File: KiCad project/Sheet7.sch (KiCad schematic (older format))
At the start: 17 parts, among them U6 AFE4403, X4 CRYSTAL_8MHZ_SMD

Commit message: New packages, PCB
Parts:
- C26: renamed from C37; footprint (none) -> Capacitors_SMD:C_0603
- C27: renamed from C38; footprint (none) -> Capacitors_SMD:C_0603
- C28, C29: renamed from C?; footprint (none) -> Capacitors_SMD:C_0603
- C30: renamed from C39; footprint (none) -> Capacitors_SMD:C_0603
- C31: renamed from C40; footprint (none) -> Capacitors_SMD:C_0603
- C32: renamed from C41; footprint (none) -> Capacitors_SMD:C_0603
- C33: renamed from C42; footprint (none) -> Capacitors_SMD:C_0603
- C34: renamed from C43; footprint (none) -> Capacitors_SMD:C_0603
- C35: renamed from C44; footprint (none) -> Capacitors_SMD:C_0603
- FB1: renamed from FB?; footprint (none) -> Capacitors_SMD:C_0603
- R7: footprint (none) -> Resistors_SMD:R_0603
- X3: renamed from X4; footprint (none) -> Anastasia:5x3.2_Crystal_SMD
- renumbered U6 to U7
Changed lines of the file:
@@
 $EndDescr
 $Comp
-L AFE4403 U6
+L AFE4403 U7
 U 1 1 5507E4DD
 P 4850 2000
-F 0 "U6" H 4900 2050 60  0000 C CNN
+F 0 "U7" H 4900 2050 60  0000 C CNN
 F 1 "AFE4403" H 6300 -350 60  0000 C CNN
 F 2 "Anastasia:DSBGA36" H 4850 2000 60  0001 C CNN
@@
 $EndComp
 $Comp
-L CRYSTAL_SMD X4
+L CRYSTAL_SMD X3
 U 1 1 5507E5E4
 P 7200 3700
-F 0 "X4" H 7200 3790 50  0000 C CNN
+F 0 "X3" H 7200 3790 50  0000 C CNN
 F 1 "CRYSTAL_8MHZ_SMD" H 7230 3590 50  0000 L CNN
-F 2 "" H 7200 3700 60  0001 C CNN
+F 2 "Anastasia:5x3.2_Crystal_SMD" H 7200 3700 60  0001 C CNN
 F 3 "" H 7200 3700 60  0000 C CNN
 	1    7200 3700
@@
 $EndComp
 $Comp
-L GND #PWR033
+L GND #PWR032
 U 1 1 5507E63E
 P 7200 4300
-F 0 "#PWR033" H 7200 4050 60  0001 C CNN
+F 0 "#PWR032" H 7200 4050 60  0001 C CNN
 F 1 "GND" H 7200 4150 60  0000 C CNN
 F 2 "" H 7200 4300 60  0000 C CNN
@@
 $EndComp
 $Comp
-L C C43
+L C C34
 U 1 1 5507E652
 P 7000 4050
-F 0 "C43" H 7050 4150 50  0000 L CNN
+F 0 "C34" H 7050 4150 50  0000 L CNN
 F 1 "C" H 7050 3950 50  0000 L CNN
-F 2 "" H 7038 3900 30  0001 C CNN
+F 2 "Capacitors_SMD:C_0603" H 7038 3900 30  0001 C CNN
 F 3 "" H 7000 4050 60  0000 C CNN
 	1    7000 4050
@@
 $EndComp
 $Comp
-L C C44
+L C C35
 U 1 1 5507E675
 P 7400 4050
-F 0 "C44" H 7450 4150 50  0000 L CNN
+F 0 "C35" H 7450 4150 50  0000 L CNN
 F 1 "C" H 7450 3950 50  0000 L CNN
-F 2 "" H 7438 3900 30  0001 C CNN
+F 2 "Capacitors_SMD:C_0603" H 7438 3900 30  0001 C CNN
 F 3 "" H 7400 4050 60  0000 C CNN
 	1    7400 4050
@@
 Choose load capacitors according \nto crystal's datasheet\n
 $Comp
-L GND #PWR034
+L GND #PWR033
 U 1 1 5507E970
 P 7050 3350
-F 0 "#PWR034" H 7050 3100 60  0001 C CNN
+F 0 "#PWR033" H 7050 3100 60  0001 C CNN
 F 1 "GND" H 7050 3200 60  0000 C CNN
 F 2 "" H 7050 3350 60  0000 C CNN
@@
 $EndComp
 $Comp
-L GND #PWR035
+L GND #PWR034
 U 1 1 5507E997
 P 6900 2800
-F 0 "#PWR035" H 6900 2550 60  0001 C CNN
+F 0 "#PWR034" H 6900 2550 60  0001 C CNN
 F 1 "GND" H 6900 2650 60  0000 C CNN
 F 2 "" H 6900 2800 60  0000 C CNN
@@
 $EndComp
 $Comp
-L +3V3 #PWR036
+L +3V3 #PWR035
 U 1 1 5507E9AF
 P 8450 2550
-F 0 "#PWR036" H 8450 2400 60  0001 C CNN
+F 0 "#PWR035" H 8450 2400 60  0001 C CNN
 F 1 "+3V3" H 8450 2690 60  0000 C CNN
 F 2 "" H 8450 2550 60  0000 C CNN
@@
 $EndComp
 $Comp
-L C C42
+L C C33
 U 1 1 5507EA21
 P 7800 3550
-F 0 "C42" H 7850 3650 50  0000 L CNN
+F 0 "C33" H 7850 3650 50  0000 L CNN
 F 1 "2.2U" H 7850 3450 50  0000 L CNN
-F 2 "" H 7838 3400 30  0001 C CNN
+F 2 "Capacitors_SMD:C_0603" H 7838 3400 30  0001 C CNN
 F 3 "" H 7800 3550 60  0000 C CNN
 	1    7800 3550
@@
 $EndComp
 $Comp
-L GND #PWR037
+L GND #PWR036
 U 1 1 5507EA5D
 P 7800 3850
-F 0 "#PWR037" H 7800 3600 60  0001 C CNN
+F 0 "#PWR036" H 7800 3600 60  0001 C CNN
 F 1 "GND" H 7800 3700 60  0000 C CNN
 F 2 "" H 7800 3850 60  0000 C CNN
@@
 $EndComp
 $Comp
-L C C40
+L C C31
 U 1 1 5507EAF1
 P 8450 2750
-F 0 "C40" H 8500 2850 50  0000 L CNN
+F 0 "C31" H 8500 2850 50  0000 L CNN
 F 1 "0.1U" H 8500 2650 50  0000 L CNN
-F 2 "" H 8488 2600 30  0001 C CNN
+F 2 "Capacitors_SMD:C_0603" H 8488 2600 30  0001 C CNN
 F 3 "" H 8450 2750 60  0000 C CNN
 	1    8450 2750
@@
 $EndComp
 $Comp
-L GND #PWR038
+L GND #PWR037
 U 1 1 5507EB22
 P 8450 3000
-F 0 "#PWR038" H 8450 2750 60  0001 C CNN
+F 0 "#PWR037" H 8450 2750 60  0001 C CNN
 F 1 "GND" H 8450 2850 60  0000 C CNN
 F 2 "" H 8450 3000 60  0000 C CNN
@@
 $EndComp
 $Comp
-L GND #PWR039
+L GND #PWR038
 U 1 1 5507EC48
 P 6950 2450
-F 0 "#PWR039" H 6950 2200 60  0001 C CNN
+F 0 "#PWR038" H 6950 2200 60  0001 C CNN
 F 1 "GND" H 6950 2300 60  0000 C CNN
 F 2 "" H 6950 2450 60  0000 C CNN
@@
 	7100 1850 7100 2650
 $Comp
-L GND #PWR041
+L GND #PWR039
 U 1 1 5507EE1C
 P 7800 2300
-F 0 "#PWR041" H 7800 2050 60  0001 C CNN
+F 0 "#PWR039" H 7800 2050 60  0001 C CNN
 F 1 "GND" H 7800 2150 60  0000 C CNN
 F 2 "" H 7800 2300 60  0000 C CNN
@@
 $EndComp
 $Comp
-L C C39
+L C C30
 U 1 1 5507EE30
 P 7800 2050
-F 0 "C39" H 7850 2150 50  0000 L CNN
+F 0 "C30" H 7850 2150 50  0000 L CNN
 F 1 "0.1U" H 7850 1950 50  0000 L CNN
-F 2 "" H 7838 1900 30  0001 C CNN
+F 2 "Capacitors_SMD:C_0603" H 7838 1900 30  0001 C CNN
 F 3 "" H 7800 2050 60  0000 C CNN
 	1    7800 2050
@@
 	7100 1850 8350 1850
 $Comp
-L C C41
+L C C32
 U 1 1 5507F067
 P 8050 3000
-F 0 "C41" H 8100 3100 50  0000 L CNN
+F 0 "C32" H 8100 3100 50  0000 L CNN
 F 1 "0.1U" H 8100 2900 50  0000 L CNN
-F 2 "" H 8088 2850 30  0001 C CNN
+F 2 "Capacitors_SMD:C_0603" H 8088 2850 30  0001 C CNN
 F 3 "" H 8050 3000 60  0000 C CNN
 	1    8050 3000
@@
 $EndComp
 $Comp
-L GND #PWR042
+L GND #PWR040
 U 1 1 5507F092
 P 8050 3250
-F 0 "#PWR042" H 8050 3000 60  0001 C CNN
+F 0 "#PWR040" H 8050 3000 60  0001 C CNN
 F 1 "GND" H 8050 3100 60  0000 C CNN
 F 2 "" H 8050 3250 60  0000 C CNN
@@
 $EndComp
 $Comp
-L +3V3 #PWR043
+L +3V3 #PWR041
 U 1 1 5507F0A6
 P 8050 2750
-F 0 "#PWR043" H 8050 2600 60  0001 C CNN
+F 0 "#PWR041" H 8050 2600 60  0001 C CNN
 F 1 "+3V3" H 8050 2890 60  0000 C CNN
 F 2 "" H 8050 2750 60  0000 C CNN
@@
 	7700 2800 8050 2800
 $Comp
-L C C37
+L C C26
 U 1 1 5507F407
 P 6850 1450
-F 0 "C37" H 6900 1550 50  0000 L CNN
+F 0 "C26" H 6900 1550 50  0000 L CNN
 F 1 "1U" H 6900 1350 50  0000 L CNN
-F 2 "" H 6888 1300 30  0001 C CNN
+F 2 "Capacitors_SMD:C_0603" H 6888 1300 30  0001 C CNN
 F 3 "" H 6850 1450 60  0000 C CNN
 	1    6850 1450
@@
 $EndComp
 $Comp
-L GND #PWR044
+L GND #PWR042
 U 1 1 5507F42E
 P 6850 1750
-F 0 "#PWR044" H 6850 1500 60  0001 C CNN
+F 0 "#PWR042" H 6850 1500 60  0001 C CNN
 F 1 "GND" H 6850 1600 60  0000 C CNN
 F 2 "" H 6850 1750 60  0000 C CNN
@@
 $EndComp
 $Comp
-L +3V3 #PWR045
+L +3V3 #PWR043
 U 1 1 5507F442
 P 6850 1150
-F 0 "#PWR045" H 6850 1000 60  0001 C CNN
+F 0 "#PWR043" H 6850 1000 60  0001 C CNN
 F 1 "+3V3" H 6850 1290 60  0000 C CNN
 F 2 "" H 6850 1150 60  0000 C CNN
@@
 	6650 1250 6850 1250
 $Comp
-L GND #PWR046
+L GND #PWR044
 U 1 1 5507FE0D
 P 3700 2300
-F 0 "#PWR046" H 3700 2050 60  0001 C CNN
+F 0 "#PWR044" H 3700 2050 60  0001 C CNN
 F 1 "GND" H 3700 2150 60  0000 C CNN
 F 2 "" H 3700 2300 60  0000 C CNN
@@
 $EndComp
 $Comp
-L C C38
+L C C27
 U 1 1 5507FE21
 P 3700 2050
-F 0 "C38" H 3750 2150 50  0000 L CNN
+F 0 "C27" H 3750 2150 50  0000 L CNN
 F 1 "2.2U" H 3750 1950 50  0000 L CNN
-F 2 "" H 3738 1900 30  0001 C CNN
+F 2 "Capacitors_SMD:C_0603" H 3738 1900 30  0001 C CNN
 F 3 "" H 3700 2050 60  0000 C CNN
 	1    3700 2050
@@
 F 0 "R7" V 3080 2350 50  0000 C CNN
 F 1 "10K" V 3007 2351 50  0000 C CNN
-F 2 "" V 2930 2350 30  0001 C CNN
+F 2 "Resistors_SMD:R_0603" V 2930 2350 30  0001 C CNN
 F 3 "" H 3000 2350 30  0000 C CNN
 	1    3000 2350
@@
 Connection ~ 3000 2600
 $Comp
-L +3V3 #PWR047
+L +3V3 #PWR045
 U 1 1 55080B5C
 P 3000 1950
-F 0 "#PWR047" H 3000 1800 60  0001 C CNN
+F 0 "#PWR045" H 3000 1800 60  0001 C CNN
 F 1 "+3V3" H 3000 2090 60  0000 C CNN
 F 2 "" H 3000 1950 60  0000 C CNN
@@
 	3000 2100 3000 1950
 $Comp
-L C C?
+L C C28
 U 1 1 550D75B9
 P 7250 2050
-F 0 "C?" H 7300 2150 50  0000 L CNN
+F 0 "C28" H 7300 2150 50  0000 L CNN
 F 1 "10N" H 7300 1950 50  0000 L CNN
-F 2 "" H 7288 1900 30  0000 C CNN
+F 2 "Capacitors_SMD:C_0603" H 7288 1900 30  0001 C CNN
 F 3 "" H 7250 2050 60  0000 C CNN
 	1    7250 2050
@@
 Connection ~ 7800 1850
 $Comp
-L FILTER FB?
+L FILTER FB1
 U 1 1 550D77C7
 P 8700 1850
-F 0 "FB?" H 8700 2000 50  0000 C CNN
+F 0 "FB1" H 8700 2000 50  0000 C CNN
 F 1 "FILTER" H 8700 1750 50  0000 C CNN
-F 2 "" H 8700 1850 60  0000 C CNN
+F 2 "Capacitors_SMD:C_0603" H 8700 1850 60  0001 C CNN
 F 3 "" H 8700 1850 60  0000 C CNN
 	1    8700 1850
@@
 $EndComp
 $Comp
-L +3V3 #PWR?
+L +3V3 #PWR046
 U 1 1 550D77E4
 P 9200 1700
-F 0 "#PWR?" H 9200 1550 60  0001 C CNN
+F 0 "#PWR046" H 9200 1550 60  0001 C CNN
 F 1 "+3V3" H 9200 1840 60  0000 C CNN
 F 2 "" H 9200 1700 60  0000 C CNN
@@
 Connection ~ 7500 2250
 $Comp
-L C C?
+L C C29
 U 1 1 550D75A0
 P 7500 2050
-F 0 "C?" H 7550 2150 50  0000 L CNN
+F 0 "C29" H 7550 2150 50  0000 L CNN
 F 1 "10N" H 7550 1950 50  0000 L CNN
-F 2 "" H 7538 1900 30  0000 C CNN
+F 2 "Capacitors_SMD:C_0603" H 7538 1900 30  0001 C CNN
 F 3 "" H 7500 2050 60  0000 C CNN
 	1    7500 2050

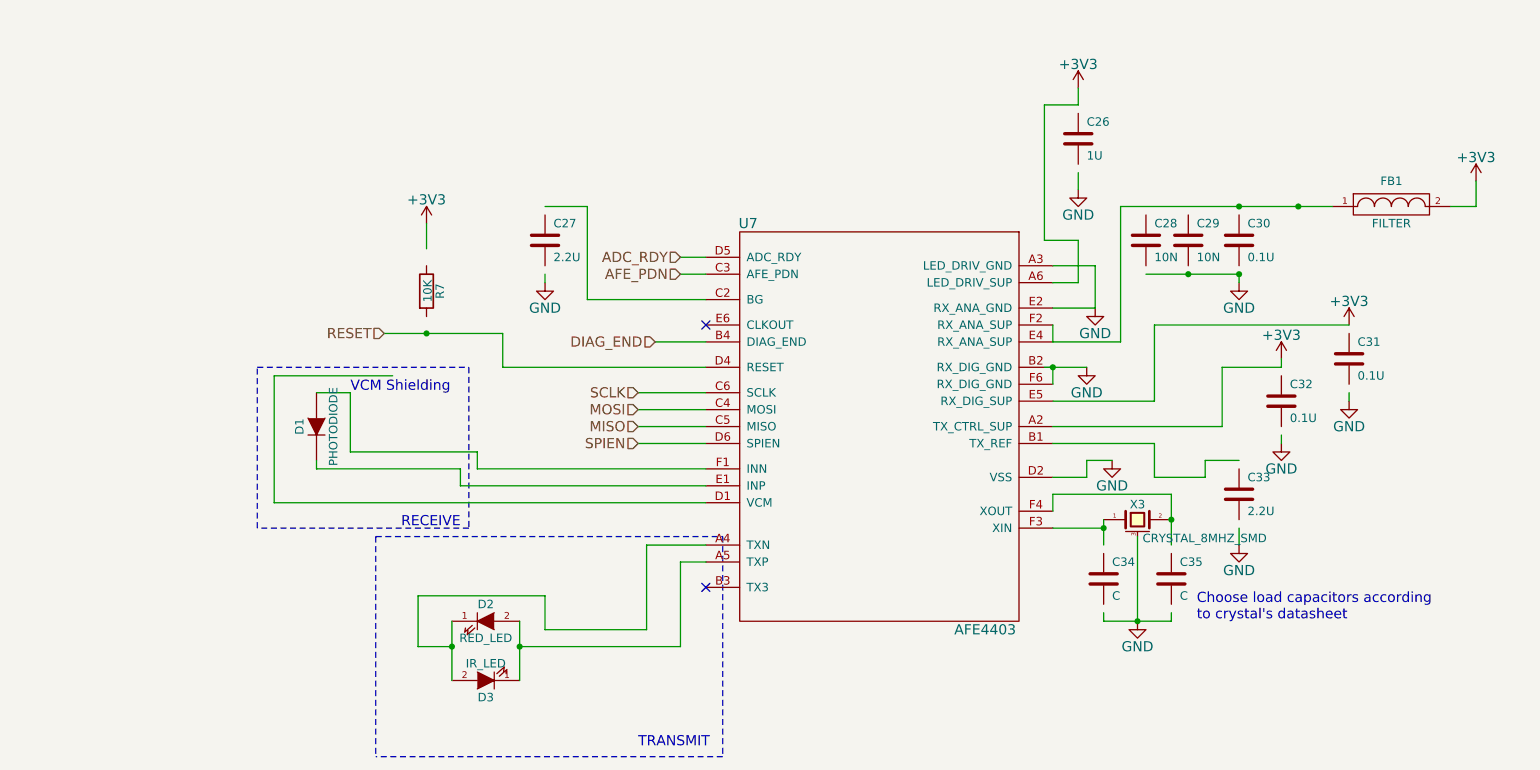
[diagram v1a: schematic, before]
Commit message: Schematics, PCB design
New schematics for the pulse oximeter, PCB layout design
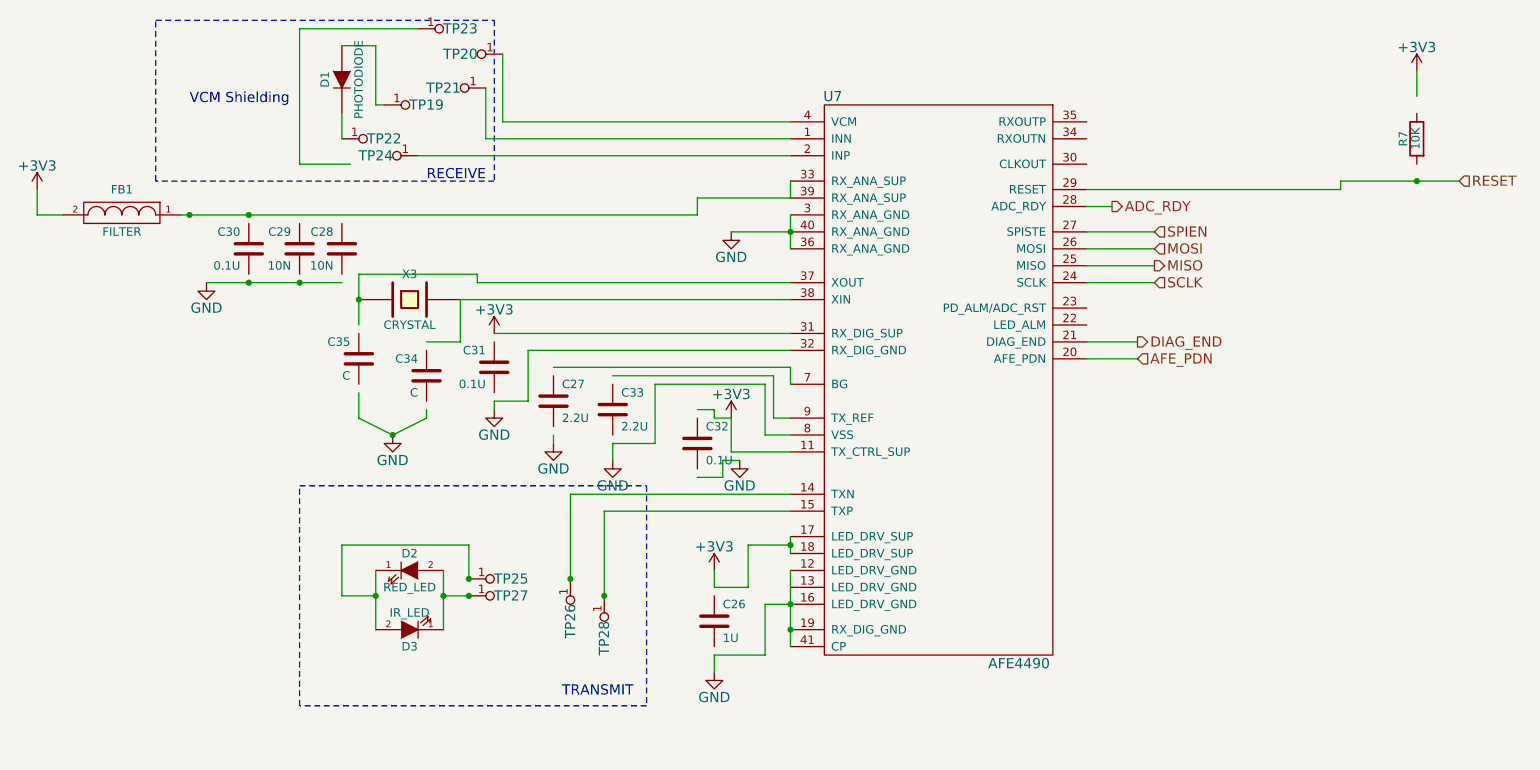
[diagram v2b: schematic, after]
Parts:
- removed U7: AFE4403, Anastasia:DSBGA36, symbol AFE4403
- removed X3: CRYSTAL_8MHZ_SMD, Anastasia:5x3.2_Crystal_SMD, symbol CRYSTAL_SMD
- added TP19, TP20, TP21, TP22, TP23, TP24, TP25, TP26, TP27, TP28: TESTPAD, Measurement_Points:Measurement_Point_Round-SMD-Pad_Small, symbol TESTPAD
- added U7: AFE4490, Anastasia:QFN40, symbol AFE4490
- added X3: CRYSTAL, Crystals:Crystal_Round_Horizontal_3mm, symbol CRYSTAL
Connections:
- wire segments 86 -> 89
- no-connect marks 2 -> 0
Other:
- note removed: "Choose load capacitors according \nto crystal's datasheet\n"
- moved on the sheet: C26, C27, C28, C29, C30, C31, C33, C34, C35, D1, D2, D3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

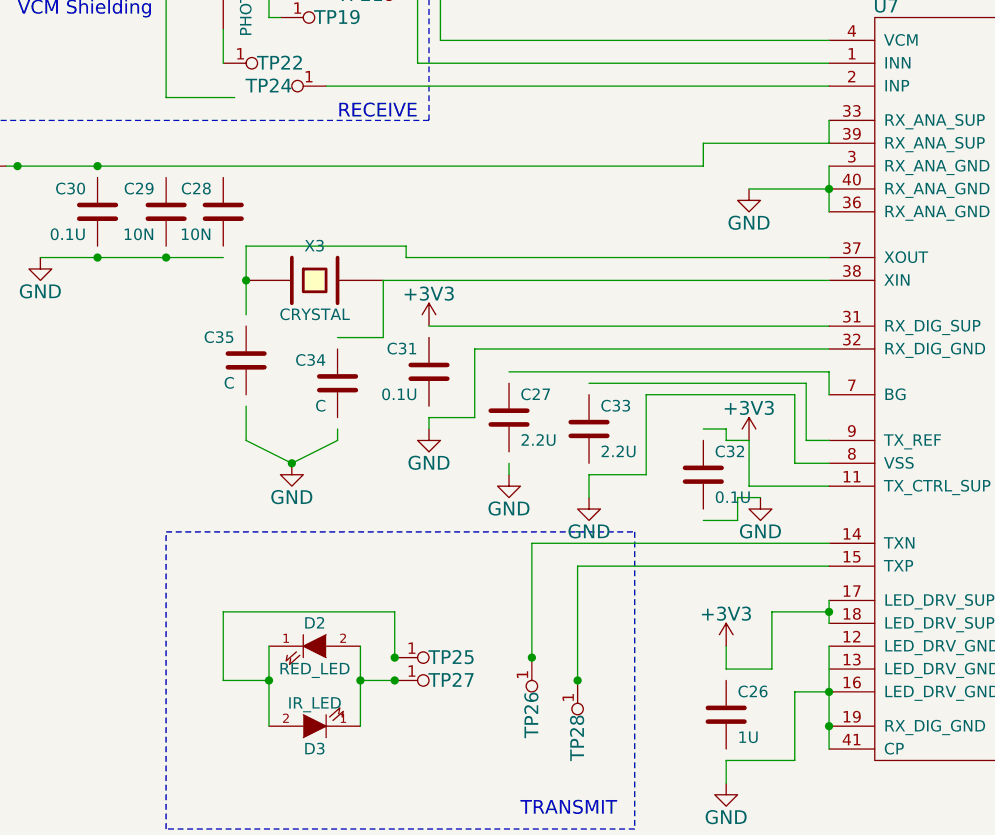
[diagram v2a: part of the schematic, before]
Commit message: PCB design
Routing for the main components, except for the power section
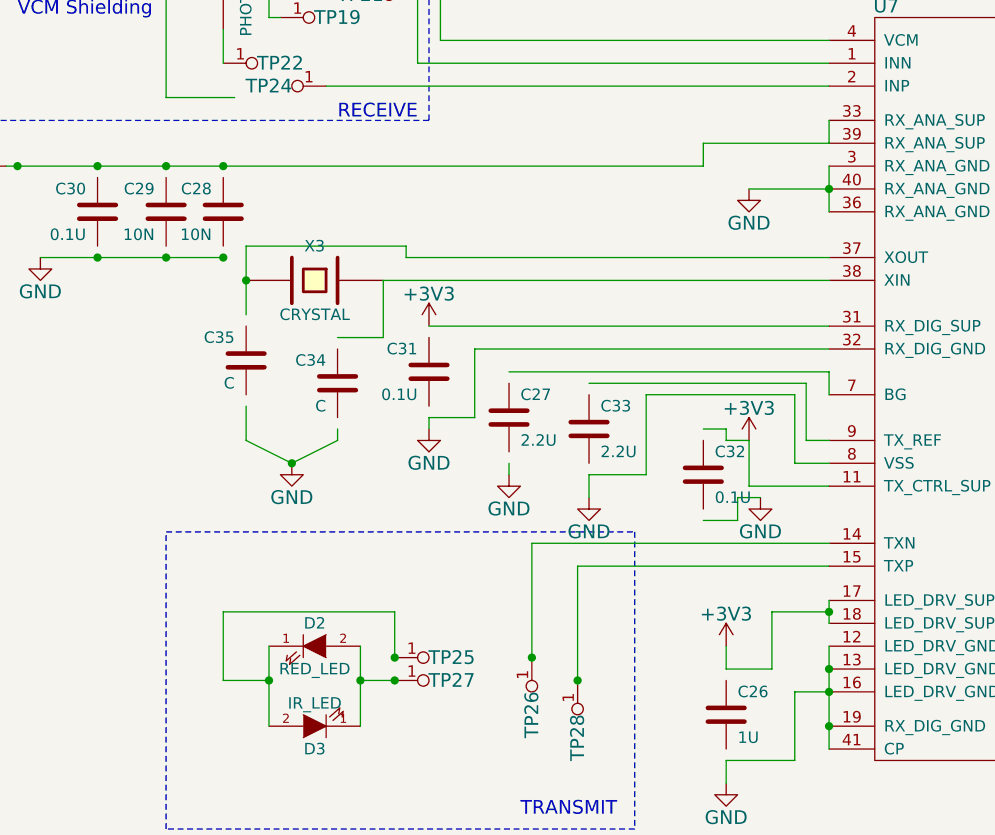
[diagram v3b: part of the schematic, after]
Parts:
- TP19, TP20, TP21, TP22, TP23, TP24, TP25, TP26, TP27, TP28: footprint Measurement_Points:Measurement_Point_Round-SMD-Pad_Small -> Anastasia:Test_Point_Round-SMD-Pad
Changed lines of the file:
@@
 F 0 "TP25" H 3500 4050 60  0000 C CNN
 F 1 "TESTPAD" H 3300 3850 60  0001 C CNN
-F 2 "Measurement_Points:Measurement_Point_Round-SMD-Pad_Small" H 3500 4050 60  0001 C CNN
+F 2 "Anastasia:Test_Point_Round-SMD-Pad" H 3500 4050 60  0001 C CNN
 F 3 "" H 3500 4050 60  0000 C CNN
 	1    3250 4050
@@
 F 0 "TP27" H 3500 4150 60  0000 C CNN
 F 1 "TESTPAD" H 3300 3950 60  0001 C CNN
-F 2 "Measurement_Points:Measurement_Point_Round-SMD-Pad_Small" H 3500 4150 60  0001 C CNN
+F 2 "Anastasia:Test_Point_Round-SMD-Pad" H 3500 4150 60  0001 C CNN
 F 3 "" H 3500 4150 60  0000 C CNN
 	1    3250 4150
@@
 F 0 "TP26" H 4100 4050 60  0000 C CNN
 F 1 "TESTPAD" H 3900 3850 60  0001 C CNN
-F 2 "Measurement_Points:Measurement_Point_Round-SMD-Pad_Small" H 4100 4050 60  0001 C CNN
+F 2 "Anastasia:Test_Point_Round-SMD-Pad" H 4100 4050 60  0001 C CNN
 F 3 "" H 4100 4050 60  0000 C CNN
 	1    3850 4050
@@
 F 0 "TP28" H 4300 4150 60  0000 C CNN
 F 1 "TESTPAD" H 4100 3950 60  0001 C CNN
-F 2 "Measurement_Points:Measurement_Point_Round-SMD-Pad_Small" H 4300 4150 60  0001 C CNN
+F 2 "Anastasia:Test_Point_Round-SMD-Pad" H 4300 4150 60  0001 C CNN
 F 3 "" H 4300 4150 60  0000 C CNN
 	1    4050 4150
@@
 F 0 "TP20" H 3700 950 60  0000 C CNN
 F 1 "TESTPAD" H 3500 750 60  0001 C CNN
-F 2 "Measurement_Points:Measurement_Point_Round-SMD-Pad_Small" H 3700 950 60  0001 C CNN
+F 2 "Anastasia:Test_Point_Round-SMD-Pad" H 3700 950 60  0001 C CNN
 F 3 "" H 3700 950 60  0000 C CNN
 	1    3450 950
@@
 F 0 "TP21" H 3600 1150 60  0000 C CNN
 F 1 "TESTPAD" H 3400 950 60  0001 C CNN
-F 2 "Measurement_Points:Measurement_Point_Round-SMD-Pad_Small" H 3600 1150 60  0001 C CNN
+F 2 "Anastasia:Test_Point_Round-SMD-Pad" H 3600 1150 60  0001 C CNN
 F 3 "" H 3600 1150 60  0000 C CNN
 	1    3350 1150
@@
 F 0 "TP24" H 3200 1550 60  0000 C CNN
 F 1 "TESTPAD" H 3000 1350 60  0001 C CNN
-F 2 "Measurement_Points:Measurement_Point_Round-SMD-Pad_Small" H 3200 1550 60  0001 C CNN
+F 2 "Anastasia:Test_Point_Round-SMD-Pad" H 3200 1550 60  0001 C CNN
 F 3 "" H 3200 1550 60  0000 C CNN
 	1    2950 1550
@@
 F 0 "TP23" H 3200 800 60  0000 C CNN
 F 1 "TESTPAD" H 3000 600 60  0001 C CNN
-F 2 "Measurement_Points:Measurement_Point_Round-SMD-Pad_Small" H 3200 800 60  0001 C CNN
+F 2 "Anastasia:Test_Point_Round-SMD-Pad" H 3200 800 60  0001 C CNN
 F 3 "" H 3200 800 60  0000 C CNN
 	1    2950 800
@@
 F 0 "TP22" H 2750 1450 60  0000 C CNN
 F 1 "TESTPAD" H 2550 1250 60  0001 C CNN
-F 2 "Measurement_Points:Measurement_Point_Round-SMD-Pad_Small" H 2750 1450 60  0001 C CNN
+F 2 "Anastasia:Test_Point_Round-SMD-Pad" H 2750 1450 60  0001 C CNN
 F 3 "" H 2750 1450 60  0000 C CNN
 	1    2500 1450
@@
 F 0 "TP19" H 3000 1250 60  0000 C CNN
 F 1 "TESTPAD" H 2800 1050 60  0001 C CNN
-F 2 "Measurement_Points:Measurement_Point_Round-SMD-Pad_Small" H 3000 1250 60  0001 C CNN
+F 2 "Anastasia:Test_Point_Round-SMD-Pad" H 3000 1250 60  0001 C CNN
 F 3 "" H 3000 1250 60  0000 C CNN
 	1    2750 1250
@@
 F 3 "" H 2900 2400 60  0000 C CNN
 	1    2900 2400
-	1    0    0    -1
+	-1   0    0    -1
 $EndComp
 Wire Wire Line
@@
 Wire Wire Line
 	3200 2650 3200 2400
+Connection ~ 2500 2300
+Connection ~ 2500 1900
+Connection ~ 2250 1900
+Connection ~ 5150 4100
 $EndSCHEMATC
